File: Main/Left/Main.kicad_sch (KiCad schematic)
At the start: 44 parts, among them SW1 RotaryEncoder_Switch_MP, SW2 Switch, U1 Arduino_Pro_Micro, U2 TRRS

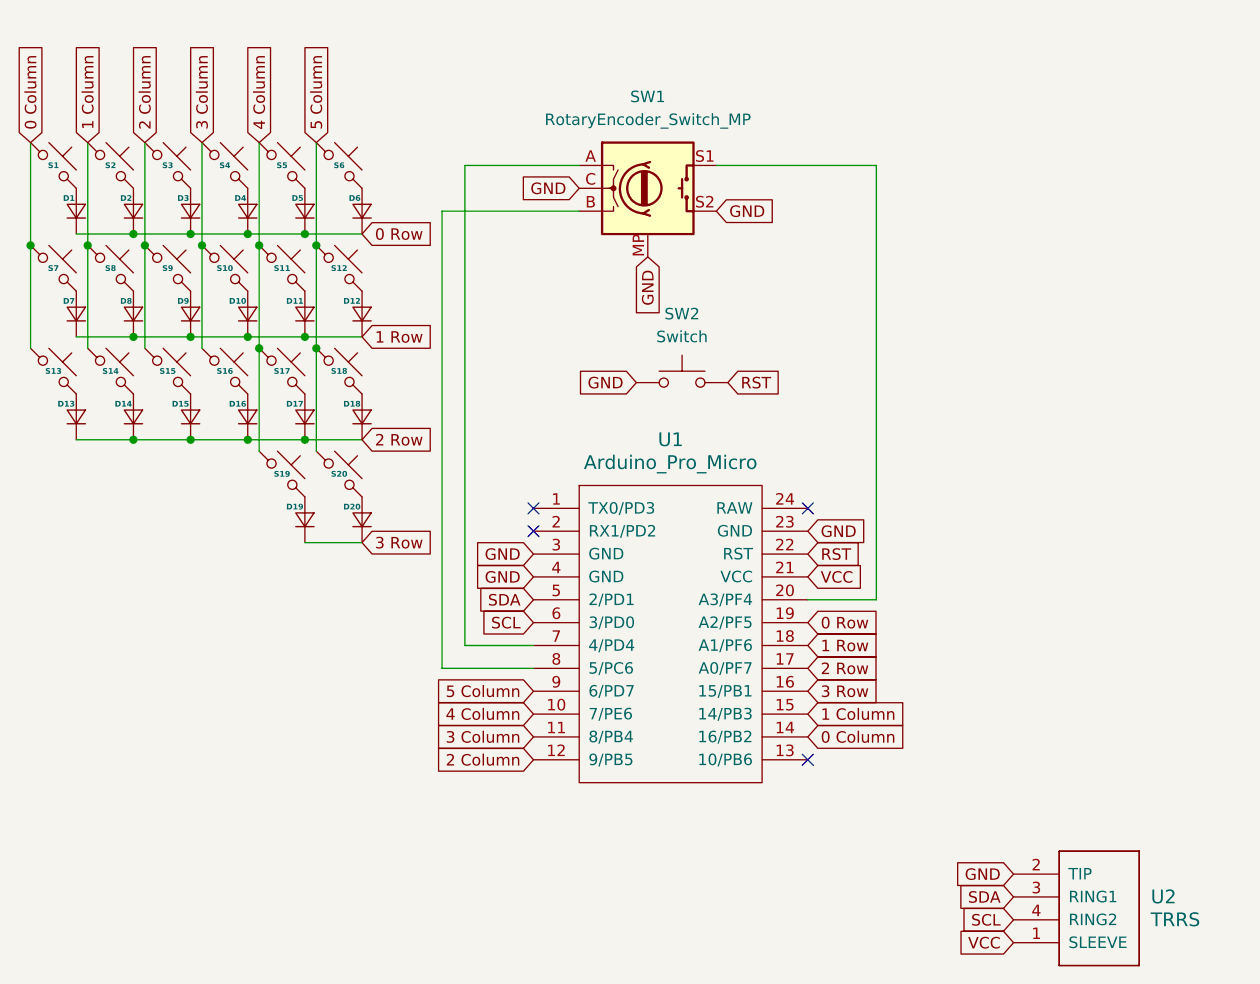
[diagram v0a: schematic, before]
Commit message: changed from I2C communication between the halves to serial because it's easier with QMK
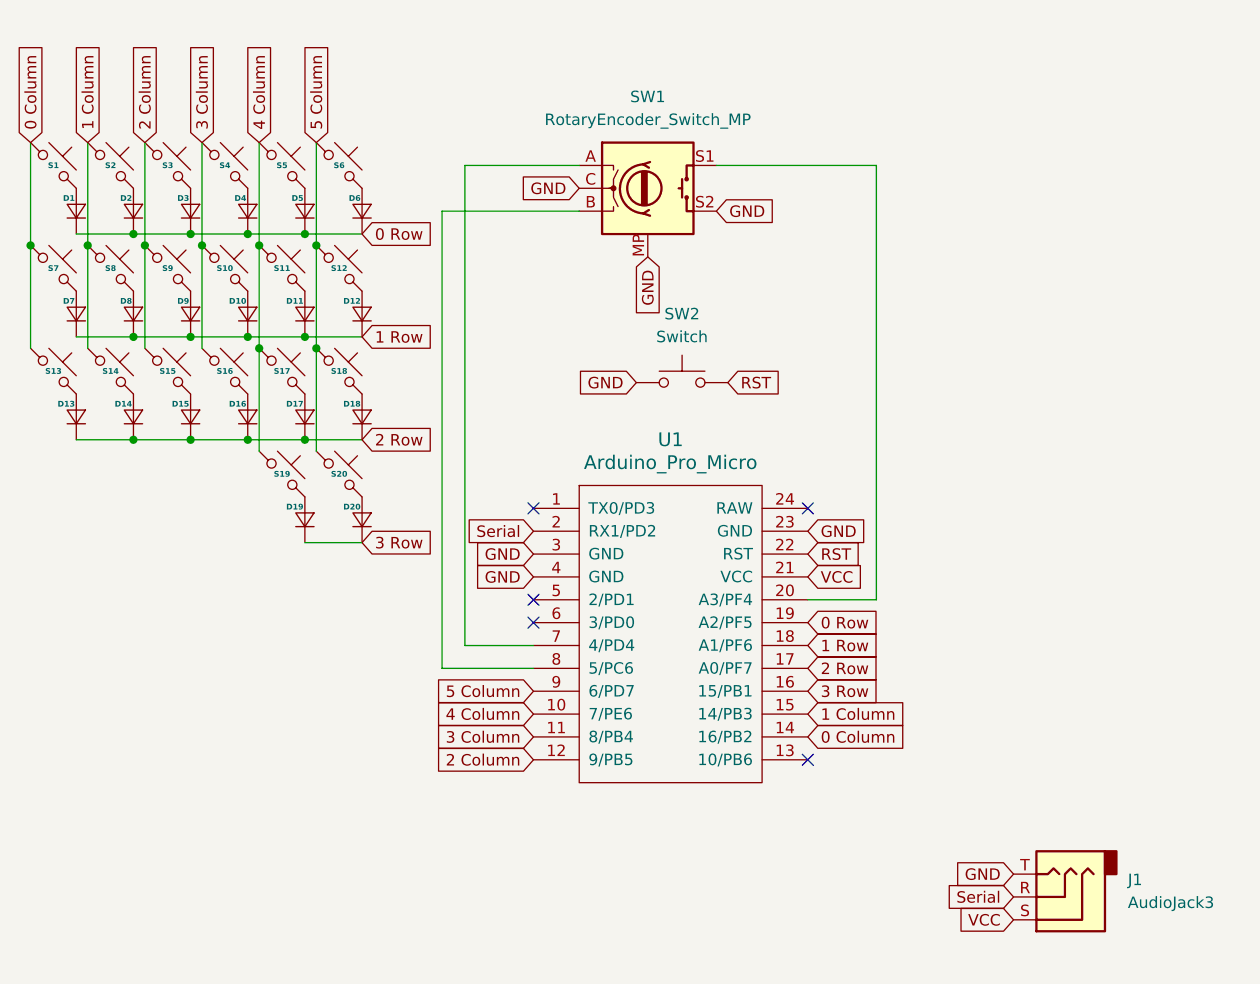
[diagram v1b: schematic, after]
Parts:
- removed U2: TRRS, ScottoKeebs_Components:TRRS_PJ-320A, symbol ScottoKeebs:Placeholder_TRRS
- added J1: AudioJack3, Connector_Audio:Jack_3.5mm_CUI_SJ1-3533NG_Horizontal_CircularHoles, symbol Connector_Audio:AudioJack3
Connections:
- net GND: now also J1.T
- net VCC: now also J1.S
- net Serial: now reaches U1.2 (RX1/PD2)
- net Serial: now also J1.R
- net SCL: no longer names the net of U1.6 (3/PD0)
- net SDA: no longer names the net of U1.5 (2/PD1)
- no-connect marks 4 -> 5
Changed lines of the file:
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@@
 	)
 	(no_connect
+		(at 111.76 100.33)
+	)
+	(no_connect
 		(at 142.24 87.63)
 	)
 	(no_connect
-		(at 111.76 90.17)
+		(at 111.76 97.79)
 	)
 	(no_connect
@@
 		)
 	)
-	(global_label "SDA"
-		(shape input)
-		(at 111.76 97.79 180)
-		(fields_autoplaced yes)
-		(effects
-			(font
-				(size 1.27 1.27)
-			)
-			(justify right)
-		)
-		(property "Intersheetrefs" "${INTERSHEET_REFS}"
-			(at 105.2067 97.79 0)
-			(effects
-				(font
-					(size 1.27 1.27)
-				)
-				(justify right)
-				(hide yes)
-			)
-		)
-	)
 	(global_label "0 Row"
 		(shape input)
@@
 	(global_label "VCC"
 		(shape input)
-		(at 165.1 135.89 180)
+		(at 165.1 133.35 180)
 		(fields_autoplaced yes)
 		(effects
@@
 		)
 		(property "Intersheetrefs" "${INTERSHEET_REFS}"
-			(at 158.4862 135.89 0)
+			(at 158.4862 133.35 0)
 			(effects
 				(font
@@
 		)
 	)
-	(global_label "SDA"
-		(shape input)
-		(at 165.1 130.81 180)
-		(fields_autoplaced yes)
-		(effects
-			(font
-				(size 1.27 1.27)
-			)
-			(justify right)
-		)
-		(property "Intersheetrefs" "${INTERSHEET_REFS}"
-			(at 158.5467 130.81 0)
-			(effects
-				(font
-					(size 1.27 1.27)
-				)
-				(justify right)
-				(hide yes)
-			)
-		)
-	)
 	(global_label "0 Column"
 		(shape input)
@@
 		)
 	)
-	(global_label "SCL"
+	(global_label "3 Row"
 		(shape input)
-		(at 165.1 133.35 180)
+		(at 92.71 91.44 0)
 		(fields_autoplaced yes)
 		(effects
@@
 				(size 1.27 1.27)
 			)
-			(justify right)
+			(justify left)
 		)
 		(property "Intersheetrefs" "${INTERSHEET_REFS}"
-			(at 158.6072 133.35 0)
+			(at 101.6218 91.44 0)
 			(effects
 				(font
 					(size 1.27 1.27)
 				)
-				(justify right)
+				(justify left)
 				(hide yes)
 			)
 		)
 	)
-	(global_label "3 Row"
+	(global_label "GND"
 		(shape input)
-		(at 92.71 91.44 0)
+		(at 142.24 90.17 0)
 		(fields_autoplaced yes)
 		(effects
@@
 		)
 		(property "Intersheetrefs" "${INTERSHEET_REFS}"
-			(at 101.6218 91.44 0)
+			(at 149.0957 90.17 0)
 			(effects
 				(font
@@
 		)
 	)
-	(global_label "GND"
+	(global_label "Serial"
 		(shape input)
-		(at 142.24 90.17 0)
+		(at 165.1 130.81 180)
 		(fields_autoplaced yes)
 		(effects
@@
 				(size 1.27 1.27)
 			)
-			(justify left)
+			(justify right)
 		)
 		(property "Intersheetrefs" "${INTERSHEET_REFS}"
-			(at 149.0957 90.17 0)
+			(at 156.6115 130.81 0)
 			(effects
 				(font
 					(size 1.27 1.27)
 				)
-				(justify left)
+				(justify right)
 				(hide yes)
 			)
@@
 		)
 	)
-	(global_label "GND"
+	(global_label "Serial"
 		(shape input)
-		(at 111.76 92.71 180)
+		(at 111.76 90.17 180)
 		(fields_autoplaced yes)
 		(effects
@@
 		)
 		(property "Intersheetrefs" "${INTERSHEET_REFS}"
-			(at 104.9043 92.71 0)
+			(at 103.2715 90.17 0)
 			(effects
 				(font
@@
 	(global_label "GND"
 		(shape input)
-		(at 123.19 73.66 180)
+		(at 111.76 92.71 180)
 		(fields_autoplaced yes)
 		(effects
@@
 		)
 		(property "Intersheetrefs" "${INTERSHEET_REFS}"
-			(at 116.3343 73.66 0)
+			(at 104.9043 92.71 0)
 			(effects
 				(font
@@
 		)
 	)
-	(global_label "SCL"
+	(global_label "GND"
 		(shape input)
-		(at 111.76 100.33 180)
+		(at 123.19 73.66 180)
 		(fields_autoplaced yes)
 		(effects
@@
 		)
 		(property "Intersheetrefs" "${INTERSHEET_REFS}"
-			(at 105.2672 100.33 0)
+			(at 116.3343 73.66 0)
 			(effects
 				(font
@@
 	)
 	(symbol
-		(lib_id "ScottoKeebs:Placeholder_TRRS")
-		(at 173.99 138.43 0)
-		(unit 1)
-		(exclude_from_sim no)
-		(in_bom yes)
-		(on_board yes)
-		(dnp no)
-		(fields_autoplaced yes)
-		(property "Reference" "U2"
-			(at 180.34 130.8099 0)
-			(effects
-				(font
-					(size 1.524 1.524)
-				)
-				(justify left)
-			)
-		)
-		(property "Value" "TRRS"
-			(at 180.34 133.3499 0)
-			(effects
-				(font
-					(size 1.524 1.524)
-				)
-				(justify left)
-			)
-		)
-		(property "Footprint" "ScottoKeebs_Components:TRRS_PJ-320A"
-			(at 177.8 138.43 0)
-			(effects
-				(font
-					(size 1.524 1.524)
-				)
-				(hide yes)
-			)
-		)
-		(property "Datasheet" ""
-			(at 177.8 138.43 0)
-			(effects
-				(font
-					(size 1.524 1.524)
-				)
-				(hide yes)
-			)
-		)
-		(property "Description" ""
-			(at 173.99 138.43 0)
-			(effects
-				(font
-					(size 1.27 1.27)
-				)
-				(hide yes)
-			)
-		)
-		(pin "3"
-		)
-		(pin "2"
-		)
-		(pin "1"
-		)
-		(pin "4"
-		)
-		(instances
-			(project ""
-				(path "/1aaa8ee2-5e2c-4c10-b7b3-8cc6d765bb1d"
-					(reference "U2")
-					(unit 1)
-				)
-			)
-		)
-	)
-	(symbol
 		(lib_id "ScottoKeebs:Placeholder_Keyswitch")
 		(at 71.12 49.53 0)
@@
 					(unit 1)
 				)
+			)
+		)
+	)
+	(symbol
+		(lib_id "Connector_Audio:AudioJack3")
+		(at 170.18 130.81 180)
+		(unit 1)
+		(exclude_from_sim no)
+		(in_bom yes)
+		(on_board yes)
+		(dnp no)
+		(fields_autoplaced yes)
+		(property "Reference" "J1"
+			(at 177.8 128.9049 0)
+			(effects
+				(font
+					(size 1.27 1.27)
+				)
+				(justify right)
+			)
+		)
+		(property "Value" "AudioJack3"
+			(at 177.8 131.4449 0)
+			(effects
+				(font
+					(size 1.27 1.27)
+				)
+				(justify right)
+			)
+		)
+		(property "Footprint" "Connector_Audio:Jack_3.5mm_CUI_SJ1-3533NG_Horizontal_CircularHoles"
+			(at 170.18 130.81 0)
+			(effects
+				(font
+					(size 1.27 1.27)
+				)
+				(hide yes)
+			)
+		)
+		(property "Datasheet" "~"
+			(at 170.18 130.81 0)
+			(effects
+				(font
+					(size 1.27 1.27)
+				)
+				(hide yes)
+			)
+		)
+		(property "Description" "Audio Jack, 3 Poles (Stereo / TRS)"
+			(at 170.18 130.81 0)
+			(effects
+				(font
+					(size 1.27 1.27)
+				)
+				(hide yes)
+			)
+		)
+		(pin "T"
+		)
+		(pin "R"
+		)
+		(pin "S"
+		)
+		(instances
+			(project ""
+				(path "/1aaa8ee2-5e2c-4c10-b7b3-8cc6d765bb1d"
+					(reference "J1")
+					(unit 1)
+				)
